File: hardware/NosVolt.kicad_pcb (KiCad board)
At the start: 4 copper layers, 145 x 60 mm, 101 parts, among them CN201 100nF, J101 INPUTS, J102 OUTPUTS, J201 BAT_SENSE, J202 BAT_NTC, J401 USB_C_Receptacle_USB2.0_16P, Q1101 2N7002, Q1102 AO4407A, Q801 2N7002, Q802 AO4407A, Q901 2N7002, Q902 AO4407A, SW101 SW_Reset, SW102 SSSS811101, U1001 INA226, U101 ESP32-S3-WROOM-1, U102 GMT028-05, U1201 INA226, U201 ADS1115IDGS, U301 MP2307DN-LF-Z, U401 AP7361-33ER-13, U402 USBLC6-2SC6, U501 INA226, U601 INA226, U701 INA226

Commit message: rc
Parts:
- added H101: MountingHole, MountingHole:MountingHole_3.2mm_M3_Pad_Via, F.Cu at (108.7, 43.8)
- added H102: MountingHole, MountingHole:MountingHole_3.2mm_M3_Pad_Via, F.Cu at (236.7, 43.8)
- added H103: MountingHole, MountingHole:MountingHole_3.2mm_M3_Pad_Via, F.Cu at (108.7, 91.8)
- added H104: MountingHole, MountingHole:MountingHole_3.2mm_M3_Pad_Via, F.Cu at (236.4, 91.8)
- moved R103 73.6 mm to (226.2, 63.0)
- moved SW101 72.5 mm to (238.7, 50.8)
- moved C101 70.6 mm to (238.7, 54.8), turned to 0 degrees
- moved R104 68.4 mm to (218.4, 63.1), turned to 180 degrees
- moved R102 62.7 mm to (238.7, 57.8), turned to 180 degrees
- moved C401 53.5 mm to (232.7, 52.4)
- moved R101 43.1 mm to (217.1, 88.2)
- moved U101 11.3 mm to (226.6, 75.7)
- moved R401 5.91 mm to (232.4, 48.2)
- moved J101 4.90 mm to (143.6, 44.3)
- moved C802 4.81 mm to (176.6, 62.2)
- moved R402 4.66 mm to (216.6, 46.5)
- moved C601 3.56 mm to (104.9, 72.6)
- moved C602 3.56 mm to (109.9, 72.6)
- moved C701 3.56 mm to (114.7, 72.6)
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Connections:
- SW102 pad 1: unconnected-(SW102-Pad1) -> /USB_LDO/USB_3V3
- U101 pad 28: unconnected-(U101-SPIIO6/GPIO35/FSPID/SUBSPID-Pad28) -> EN_OUT1
- U101 pad 29: unconnected-(U101-SPIIO7/GPIO36/FSPICLK/SUBSPICLK-Pad29) -> EN_OUT2
- U101 pad 30: unconnected-(U101-SPIDQS/GPIO37/FSPIQ/SUBSPIQ-Pad30) -> EN_OUT3
- U101 pad 4: EN_OUT1 -> unconnected-(U101-GPIO4/TOUCH4/ADC1_CH3-Pad4)
- U101 pad 5: EN_OUT2 -> unconnected-(U101-GPIO5/TOUCH5/ADC1_CH4-Pad5)
- U101 pad 6: EN_OUT3 -> unconnected-(U101-GPIO6/TOUCH6/ADC1_CH5-Pad6)
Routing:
- net +3.3V: track 50.8 -> 347.6 mm, vias 0 -> 9
- net SDA: track 0.00 -> 198.1 mm, vias 0 -> 9
- net SCL: track 0.00 -> 186.6 mm, vias 0 -> 6
- net +12V_UPS: track 70.6 -> 196.7 mm, vias 2 -> 4
- net EN_OUT3: track 0.00 -> 97.2 mm
- net GND: track 47.5 -> 123.1 mm, vias 4 -> 10
- net EN_OUT2: track 0.00 -> 73.5 mm
- net EN_OUT1: track 0.00 -> 49.6 mm
- net /USB_LDO/USB_3V3: track 13.3 -> 43.1 mm
- net /Output3/VOUT: track 5.14 -> 32.4 mm, vias 0 -> 2
- net /MP2307/OUT: track 25.6 -> 52.7 mm, vias 2 -> 4
- net /Output2/VOUT: track 0.00 -> 26.9 mm
- net /INA226_BAT/VIN: track 14.3 -> 41.1 mm
- net /INA226_IN/VIN: track 14.3 -> 40.8 mm
- net /INA226_BAT/VOUT: track 4.29 -> 30.7 mm
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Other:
- board size 145 x 60 mm -> 140 x 60 mm
- board text added: "BAT1"
- board text added: "BAT2"
- board text added: "BAT3"
- board text added: "NTC1"
- board text added: "NTC2"

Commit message: 100*100
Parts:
- moved U101 94.2 mm to (140.4, 113.9), turned to 180 degrees
- moved U102 88.9 mm to (262.0, 72.8)
- moved C301 85.5 mm to (108.1, 85.5)
- moved C302 85.5 mm to (108.1, 90.2)
- moved C305 85.5 mm to (108.1, 80.0)
- moved R301 85.5 mm to (119.6, 92.8)
- moved C303 85.5 mm to (119.7, 88.3)
- moved C304 85.5 mm to (115.8, 88.3)
- moved R302 85.5 mm to (115.8, 92.8)
- moved R304 85.5 mm to (112.3, 88.7)
- moved L301 85.5 mm to (121.0, 82.0)
- moved R303 85.5 mm to (112.4, 92.7)
- moved U301 85.5 mm to (113.2, 82.0)
- moved C101 81.2 mm to (169.2, 96.8)
- moved R102 81.2 mm to (169.2, 99.8)
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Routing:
- net +3.3V: track 347.6 -> 53.4 mm, vias 9 -> 0
- net SDA: track 198.1 -> 4.63 mm, vias 9 -> 2
- net SCL: track 186.6 -> 0.00 mm, vias 6 -> 0
- net +12V_UPS: track 196.7 -> 26.5 mm, vias 4 -> 0
- net EN_OUT3: track 97.2 -> 0.00 mm
- net GND: track 123.1 -> 34.8 mm, vias 10 -> 4
- net EN_OUT2: track 73.5 -> 0.00 mm
- net /MP2307/OUT: track 52.7 -> 0.00 mm, vias 4 -> 0
- net EN_OUT1: track 49.6 -> 0.00 mm
- net /USB_LDO/USB_3V3: track 43.1 -> 0.00 mm
- net /INA226_BAT/VIN: track 41.1 -> 7.43 mm
- net /INA226_IN/VIN: track 40.8 -> 7.35 mm
- net /Output3/VOUT: track 32.4 -> 0.00 mm, vias 2 -> 0
- net /INA226_BAT/VOUT: track 30.7 -> 0.00 mm
- net /Output1/VOUT: track 30.5 -> 0.00 mm
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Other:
- board size 140 x 60 mm -> 100 x 60 mm

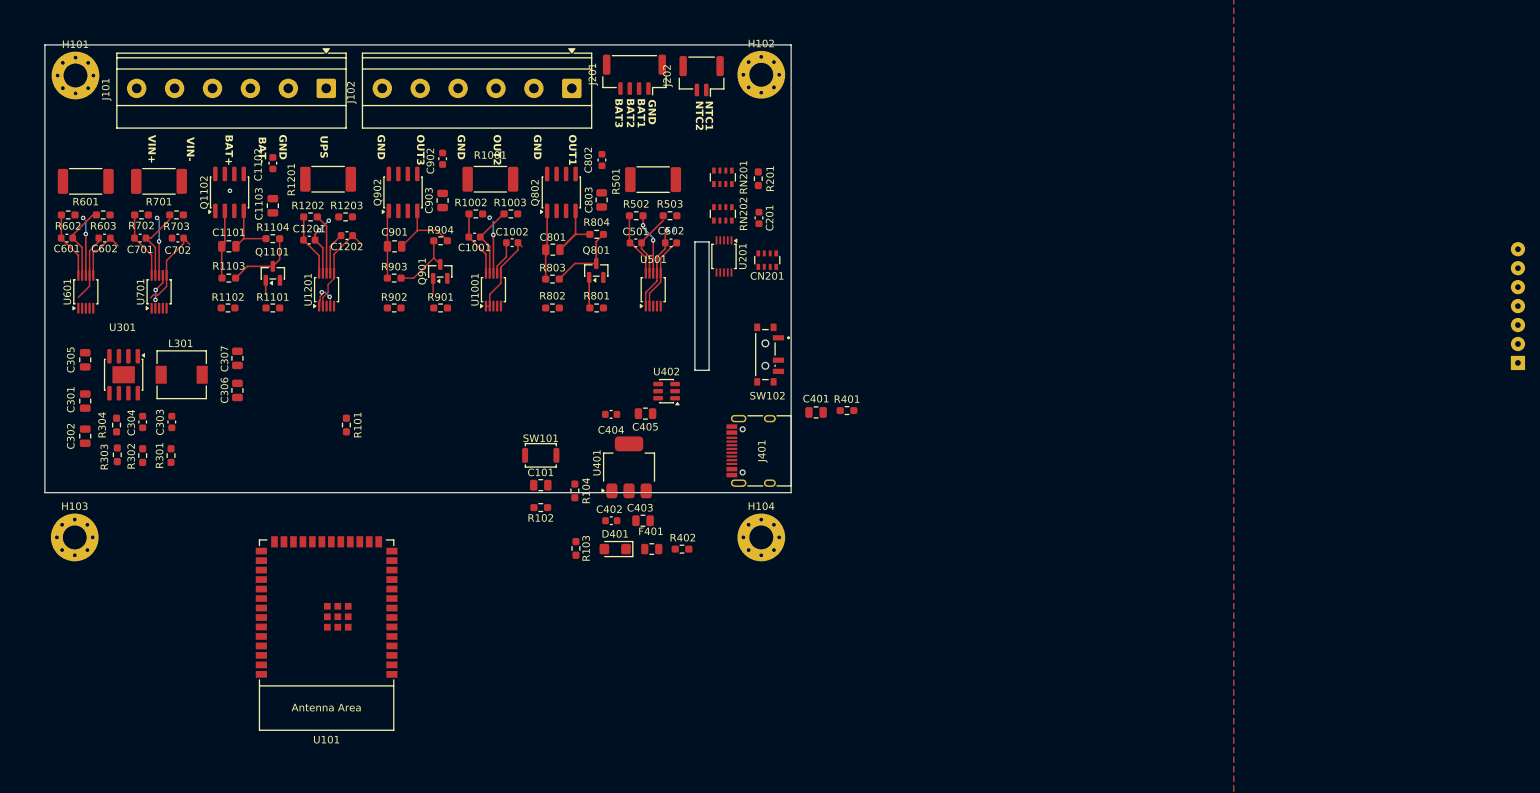
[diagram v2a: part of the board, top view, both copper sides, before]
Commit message: esp32 c3 mini
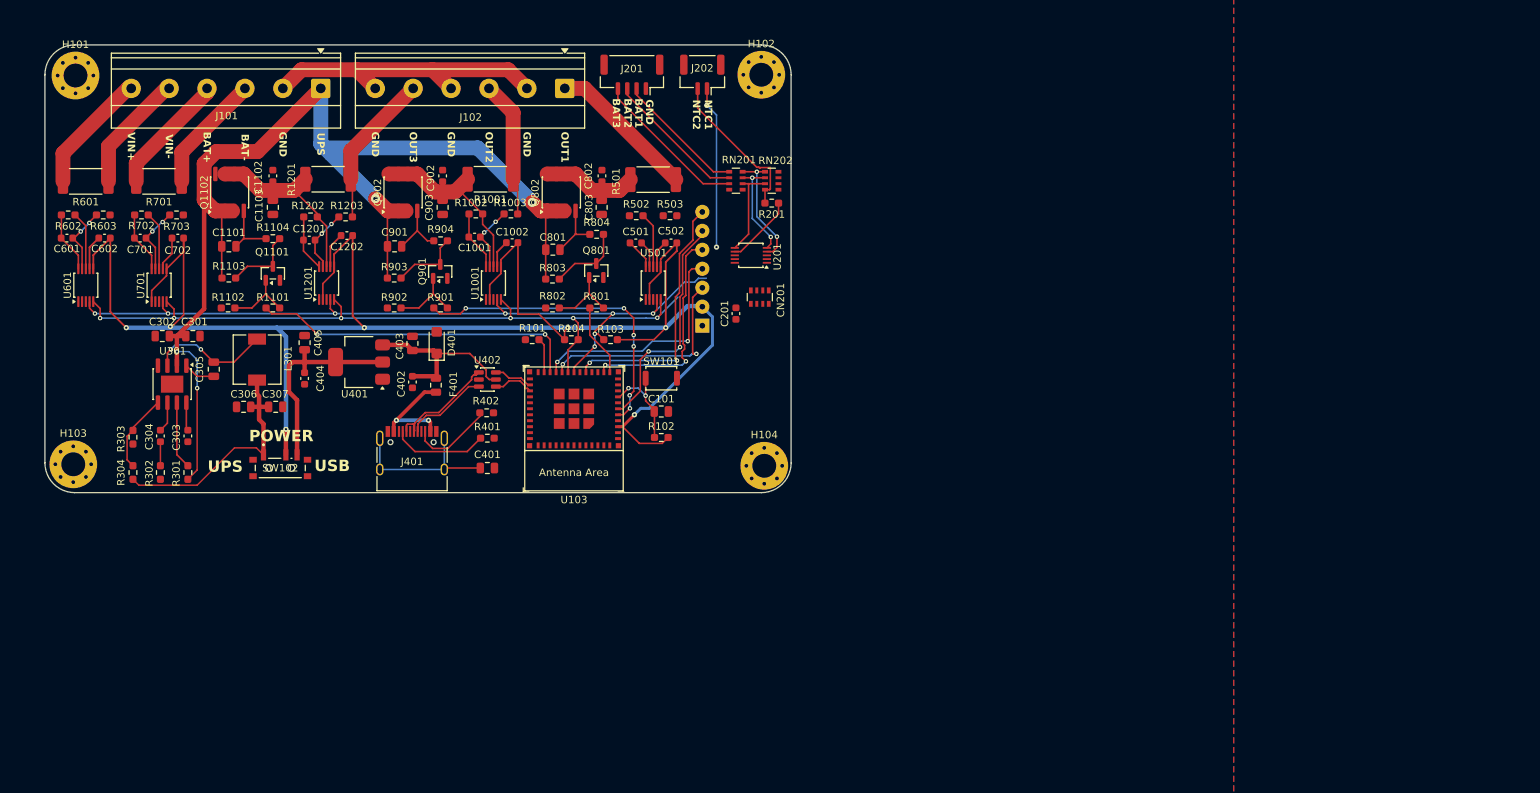
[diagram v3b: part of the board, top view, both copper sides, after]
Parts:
- removed U101: ESP32-S3-WROOM-1, PCM_Espressif:ESP32-S3-WROOM-1
- added U103: ESP32-C3-MINI-1, PCM_Espressif:ESP32-C3-MINI-1, F.Cu at (173.6, 89.3)
- moved U102 109.4 mm to (152.7, 67.8)
- moved SW102 66.8 mm to (134.2, 94.5), turned to 0 degrees
- moved R401 48.3 mm to (162.0, 90.5), turned to 0 degrees
- moved J401 46.9 mm to (151.9, 93.6), turned to 0 degrees
- moved C405 46.7 mm to (137.5, 77.7), turned to 90 degrees
- moved C401 44.7 mm to (162.0, 94.5), turned to 0 degrees
- moved C404 41.4 mm to (137.5, 82.5), turned to -90 degrees
- moved C403 39.0 mm to (151.9, 77.8), turned to 90 degrees
- moved U401 38.8 mm to (144.8, 80.3), turned to 180 degrees
- moved D401 36.6 mm to (155.2, 77.7), turned to 90 degrees
- moved F401 36.3 mm to (155.1, 83.4), turned to 90 degrees
- moved C402 32.5 mm to (151.9, 83.0), turned to -90 degrees
- moved R402 31.9 mm to (161.9, 87.1), turned to 0 degrees
- moved R103 28.4 mm to (178.5, 77.3), turned to 180 degrees
- moved R101 27.4 mm to (168.0, 77.3), turned to 180 degrees
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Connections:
- SW102 pad 1: /USB_LDO/USB_3V3 -> /MP2307/OUT
- SW102 pad 3: /MP2307/OUT -> /USB_LDO/USB_3V3
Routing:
- net +3.3V: track 53.4 -> 269.3 mm, vias 0 -> 9
- net +12V_UPS: track 26.5 -> 161.1 mm, vias 0 -> 4
- net SDA: track 4.63 -> 105.8 mm, vias 2 -> 8
- net SCL: track 0.00 -> 100.5 mm, vias 0 -> 6
- net EN_OUT3: track 0.00 -> 44.2 mm, vias 0 -> 2
- net EN_OUT2: track 0.00 -> 42.3 mm, vias 0 -> 6
- net SPI_CS_TFT: track 0.00 -> 34.8 mm, vias 0 -> 2
- net /MP2307/OUT: track 0.00 -> 33.1 mm
- net SPI_MOSI: track 0.00 -> 31.4 mm, vias 0 -> 2
- net TFT_DC: track 0.00 -> 31.0 mm, vias 0 -> 2
- net SPI_SCLK: track 0.00 -> 29.4 mm, vias 0 -> 2
- net TFT_RST: track 0.00 -> 29.3 mm, vias 0 -> 2
- net GND: track 34.8 -> 63.2 mm, vias 4 -> 0
- net /USB_LDO/USB_3V3: track 0.00 -> 28.2 mm
- net /USB_LDO/USB_5V: track 0.00 -> 24.2 mm
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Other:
- outline, holes or cut-outs redrawn
- board text added: "POWER"
- board text added: "USB"

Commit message: thermal relief
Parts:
- removed C1103, C803, C903: 22uF, Capacitor_SMD:C_0805_2012Metric
- removed U103: ESP32-C3-MINI-1, PCM_Espressif:ESP32-C3-MINI-1
- added C102: 100nF, Capacitor_SMD:C_0603_1608Metric, F.Cu at (139.6, 88.0)
- added C103: 22uF, Capacitor_SMD:C_0805_2012Metric, F.Cu at (143.4, 87.9)
- added NT1001: NetTie_SHUNT_IN_SENSE, NetTie:NetTie-2_SMD_Pad0.5mm, F.Cu at (173.6, 56.3)
- added NT1002: NetTie_SHUNT_OUT_SENSE, NetTie:NetTie-2_SMD_Pad0.5mm, F.Cu at (179.6, 56.6)
- added NT101: NetTie_OUT_12V, NetTie:NetTie-2_SMD_Pad0.5mm, F.Cu at (161.3, 58.6)
- added NT1201: NetTie_SHUNT_IN_SENSE, NetTie:NetTie-2_SMD_Pad0.5mm, F.Cu at (152.7, 56.7)
- added NT1202: NetTie_SHUNT_OUT_SENSE, NetTie:NetTie-2_SMD_Pad0.5mm, F.Cu at (157.8, 56.3)
- added NT301: NetTie_SW_BS, NetTie:NetTie-2_SMD_Pad0.5mm, F.Cu at (183.7, 80.7)
- added NT302: NetTie_SW_FB, NetTie:NetTie-2_SMD_Pad0.5mm, F.Cu at (182.9, 86.5)
- added NT303: NetTie_IN_EN, NetTie:NetTie-2_SMD_Pad0.5mm, F.Cu at (185.6, 78.3)
- added NT304: NetTie_GND, NetTie:NetTie-2_SMD_Pad0.5mm, F.Cu at (188.8, 82.0)
- added NT501: NetTie_SHUNT_IN_SENSE, NetTie:NetTie-2_SMD_Pad0.5mm, F.Cu at (195.9, 56.7)
- added NT502: NetTie_SHUNT_OUT_SENSE, NetTie:NetTie-2_SMD_Pad0.5mm, F.Cu at (200.8, 56.4)
- added NT601: NetTie_SHUNT_IN_SENSE, NetTie:NetTie-2_SMD_Pad0.5mm, F.Cu at (121.3, 56.3)
- added NT602: NetTie_SHUNT_OUT_SENSE, NetTie:NetTie-2_SMD_Pad0.5mm, F.Cu at (127.9, 56.3)
- added NT701: NetTie_SHUNT_IN_SENSE, NetTie:NetTie-2_SMD_Pad0.5mm, F.Cu at (131.3, 55.3)
- added NT702: NetTie_SHUNT_OUT_SENSE, NetTie:NetTie-2_SMD_Pad0.5mm, F.Cu at (137.4, 55.5)
- added U101: GMT028-05, NosLib:GMT028-05, F.Cu at (49.1, 81.8)
- C1101, C801, C901: value 22nF -> 100nF; footprint Capacitor_SMD:C_0805_2012Metric -> Capacitor_SMD:C_0603_1608Metric
- C1102, C802, C902: value 100nF -> 22uF; footprint Capacitor_SMD:C_0603_1608Metric -> Capacitor_SMD:C_0805_2012Metric
- U102: value GMT028-05 -> ESP32-S3-WROOM-1; footprint NosLib:GMT028-05 -> PCM_Espressif:ESP32-S3-WROOM-1; moved to F.Cu
- U301: footprint Package_SO:SOIC-8-1EP_3.9x4.9mm_P1.27mm_EP2.29x3mm -> Package_SO:SOIC-8-1EP_3.9x4.9mm_P1.27mm_EP2.29x3mm_ThermalVias
- moved U201 92.0 mm to (105.3, 65.2), turned to -90 degrees
- moved R201 90.1 mm to (110.0, 58.3)
- moved RN201 90.0 mm to (105.3, 53.7)
- moved RN202 90.0 mm to (110.1, 53.7)
- moved CN201 88.8 mm to (110.1, 62.8), turned to 0 degrees
- moved R303 86.2 mm to (200.6, 86.5), turned to 180 degrees
- moved C201 85.4 mm to (110.2, 67.4), turned to 0 degrees
- moved R302 83.4 mm to (200.6, 82.5), turned to 180 degrees
- moved R304 81.8 mm to (195.8, 86.5), turned to 0 degrees
- moved R301 80.5 mm to (200.6, 78.5), turned to 180 degrees
- moved C304 78.0 mm to (195.8, 82.5), turned to 0 degrees
- moved C303 74.9 mm to (195.8, 78.5), turned to 0 degrees
- moved C305 70.8 mm to (195.8, 74.9), turned to 180 degrees
- moved U301 70.0 mm to (189.7, 80.5), turned to 0 degrees
- moved J202 65.8 mm to (125.0, 41.2)
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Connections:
- net +3.3V renamed +3V3
- C1101 pad 1: Net-(Q1102-G) -> /Output3/SHUNT_DRAIN
- C1101 pad 2: +12V_UPS -> GND
- C1102 pad 1: /Output3/INA226_OUT/VIN -> /Output3/SHUNT_DRAIN
- C301 pad 1: +12V_UPS -> /+12V_UPS
- C301 pad 2: GND -> /MP2307/PWR_GND
- C302 pad 1: +12V_UPS -> /+12V_UPS
- C302 pad 2: GND -> /MP2307/PWR_GND
- C305 pad 2: Net-(U301-SW) -> Net-(C305-Pad2)
- C306 pad 1: /MP2307/OUT -> +3V3_UPS
- C306 pad 2: GND -> /MP2307/PWR_GND
- C307 pad 1: /MP2307/OUT -> +3V3_UPS
- C307 pad 2: GND -> /MP2307/PWR_GND
- C404 pad 1: /USB_LDO/USB_3V3 -> +3V3_USB
- C405 pad 1: /USB_LDO/USB_3V3 -> +3V3_USB
- C801 pad 1: Net-(Q802-G) -> /Output1/SHUNT_DRAIN
- C801 pad 2: +12V_UPS -> GND
- C802 pad 1: /Output1/INA226_OUT/VIN -> /Output1/SHUNT_DRAIN
- C901 pad 1: Net-(Q902-G) -> /Output2/SHUNT_DRAIN
- C901 pad 2: +12V_UPS -> GND
- C902 pad 1: /Output2/INA226_OUT/VIN -> /Output2/SHUNT_DRAIN
- J101 pad 1: +12V_UPS -> /SHUNT_OUT_LO
- J101 pad 2: GND -> /SHUNT_OUT_HI
- J101 pad 3: /INA226_BAT/VOUT -> /SHUNT_BAT_LO
- J101 pad 4: /INA226_BAT/VIN -> /SHUNT_BAT_HI
- J101 pad 5: /INA226_IN/VOUT -> /SHUNT_IN_LO
- J101 pad 6: /INA226_IN/VIN -> /SHUNT_IN_HI
- J102 pad 2: GND -> /SHUNT_OUT_HI
- J102 pad 4: GND -> /SHUNT_OUT_HI
- J102 pad 6: GND -> /SHUNT_OUT_HI
- L301 pad 1: Net-(U301-SW) -> /MP2307/SW
- L301 pad 2: /MP2307/OUT -> +3V3_UPS
- Q1102 pad 1: +12V_UPS -> /SHUNT_OUT_LO
- Q1102 pad 2: +12V_UPS -> /SHUNT_OUT_LO
- Q1102 pad 3: +12V_UPS -> /SHUNT_OUT_LO
- Q1102 pad 5: /Output3/INA226_OUT/VIN -> /Output3/SHUNT_DRAIN
- Q1102 pad 6: /Output3/INA226_OUT/VIN -> /Output3/SHUNT_DRAIN
- Q1102 pad 7: /Output3/INA226_OUT/VIN -> /Output3/SHUNT_DRAIN
- Q1102 pad 8: /Output3/INA226_OUT/VIN -> /Output3/SHUNT_DRAIN
- Q802 pad 1: +12V_UPS -> /SHUNT_OUT_LO
- Q802 pad 2: +12V_UPS -> /SHUNT_OUT_LO
- Q802 pad 3: +12V_UPS -> /SHUNT_OUT_LO
- Q802 pad 5: /Output1/INA226_OUT/VIN -> /Output1/SHUNT_DRAIN
- Q802 pad 6: /Output1/INA226_OUT/VIN -> /Output1/SHUNT_DRAIN
- Q802 pad 7: /Output1/INA226_OUT/VIN -> /Output1/SHUNT_DRAIN
- Q802 pad 8: /Output1/INA226_OUT/VIN -> /Output1/SHUNT_DRAIN
- Q902 pad 1: +12V_UPS -> /SHUNT_OUT_LO
- Q902 pad 2: +12V_UPS -> /SHUNT_OUT_LO
- Q902 pad 3: +12V_UPS -> /SHUNT_OUT_LO
- Q902 pad 5: /Output2/INA226_OUT/VIN -> /Output2/SHUNT_DRAIN
- Q902 pad 6: /Output2/INA226_OUT/VIN -> /Output2/SHUNT_DRAIN
- Q902 pad 7: /Output2/INA226_OUT/VIN -> /Output2/SHUNT_DRAIN
- Q902 pad 8: /Output2/INA226_OUT/VIN -> /Output2/SHUNT_DRAIN
- R1001 pad 2: /Output2/INA226_OUT/VIN -> /Output2/SHUNT_DRAIN
- R1002 pad 1: /Output2/INA226_OUT/VIN -> Net-(U1001-Vbus)
- R1003 pad 1: /Output2/VOUT -> Net-(NT1002-Pad2)
- R1103 pad 2: +12V_UPS -> /SHUNT_OUT_LO
- R1201 pad 2: /Output3/INA226_OUT/VIN -> /Output3/SHUNT_DRAIN
- R1202 pad 1: /Output3/INA226_OUT/VIN -> Net-(U1201-Vbus)
- R1203 pad 1: /Output3/VOUT -> Net-(NT1202-Pad2)
- R301 pad 1: +12V_UPS -> Net-(NT303-Pad2)
- R304 pad 2: /MP2307/OUT -> Net-(NT302-Pad1)
- R501 pad 2: /Output1/INA226_OUT/VIN -> /Output1/SHUNT_DRAIN
- R502 pad 1: /Output1/INA226_OUT/VIN -> Net-(U501-Vbus)
- R503 pad 1: /Output1/VOUT -> Net-(NT502-Pad2)
- R601 pad 1: /INA226_IN/VOUT -> /SHUNT_IN_LO
- R601 pad 2: /INA226_IN/VIN -> /SHUNT_IN_HI
- R602 pad 1: /INA226_IN/VIN -> Net-(U601-Vbus)
- R603 pad 1: /INA226_IN/VOUT -> Net-(NT602-Pad2)
- R701 pad 1: /INA226_BAT/VOUT -> /SHUNT_BAT_LO
- R701 pad 2: /INA226_BAT/VIN -> /SHUNT_BAT_HI
- R702 pad 1: /INA226_BAT/VIN -> Net-(U701-Vbus)
- R703 pad 1: /INA226_BAT/VOUT -> Net-(NT702-Pad2)
- R803 pad 2: +12V_UPS -> /SHUNT_OUT_LO
- R903 pad 2: +12V_UPS -> /SHUNT_OUT_LO
- SW102 pad 1: /MP2307/OUT -> +3V3_USB
- SW102 pad 3: /USB_LDO/USB_3V3 -> +3V3_UPS
- U1001 pad 8: /Output2/INA226_OUT/VIN -> Net-(U1001-Vbus)
- U102 pad 3: SPI_SCLK -> EN
- U102 pad 4: SPI_MOSI -> EN_OUT3
- U102 pad 5: TFT_RST -> EN_OUT2
- U102 pad 6: TFT_DC -> EN_OUT1
- U102 pad 7: SPI_CS_TFT -> unconnected-(U102-GPIO7/TOUCH7/ADC1_CH6-Pad7)
- U1201 pad 8: /Output3/INA226_OUT/VIN -> Net-(U1201-Vbus)
- U301 pad 2: +12V_UPS -> /+12V_UPS
- U301 pad 3: Net-(U301-SW) -> /MP2307/SW
- U301 pad 9: GND -> /MP2307/PWR_GND
- U401 pad 2: /USB_LDO/USB_3V3 -> +3V3_USB
- U501 pad 8: /Output1/INA226_OUT/VIN -> Net-(U501-Vbus)
- U601 pad 8: /INA226_IN/VIN -> Net-(U601-Vbus)
- U701 pad 8: /INA226_BAT/VIN -> Net-(U701-Vbus)
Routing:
- net +12V_UPS: track 161.1 -> 0.00 mm, vias 4 -> 0
- net +3V3: track 269.3 -> 159.8 mm, vias 9 -> 6
- net EN_OUT3: track 44.2 -> 0.00 mm, vias 2 -> 0
- net EN_OUT2: track 42.3 -> 0.00 mm, vias 6 -> 0
- net /SHUNT_OUT_HI: track 0.00 -> 41.8 mm
- net /SHUNT_OUT_LO: track 0.00 -> 41.7 mm, vias 0 -> 2
- net /+12V_UPS: track 0.00 -> 39.6 mm
- net /MP2307/OUT: track 33.1 -> 0.00 mm
- net GND: track 63.2 -> 31.2 mm, vias 0 -> 2
- net SCL: track 100.5 -> 130.4 mm, vias 6 -> 7
- net /USB_LDO/USB_3V3: track 28.2 -> 0.00 mm
- net /Output2/INA226_OUT/VIN: track 27.3 -> 0.00 mm
- net /Output3/INA226_OUT/VIN: track 26.8 -> 0.00 mm
- net /INA226_IN/VIN: track 24.3 -> 0.00 mm
- net /USB_LDO/USB_5V: track 24.2 -> 0.00 mm
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- added copper zone on F.Cu, net /MP2307/PWR_GND
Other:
- outline, holes or cut-outs redrawn

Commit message: optimization
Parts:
- moved R304 6.54 mm to (189.3, 86.2), turned to -90 degrees
- moved R303 5.75 mm to (194.9, 86.2), turned to 90 degrees
- moved R302 4.98 mm to (198.6, 87.1), turned to 0 degrees
- moved C303 4.26 mm to (198.6, 75.2)
- moved C307 3.40 mm to (179.3, 90.7), turned to -90 degrees
- moved C304 2.80 mm to (198.6, 83.1)
- moved NT301 2.56 mm to (186.3, 80.6)
- moved C301 2.56 mm to (182.9, 76.2)
- moved C302 2.56 mm to (186.6, 76.2)
- moved L301 2.56 mm to (184.3, 84.0)
- moved NT302 2.56 mm to (185.5, 86.5)
- moved NT304 2.56 mm to (191.4, 82.0)
- moved U301 2.56 mm to (192.3, 80.5)
- moved R301 2.14 mm to (198.6, 79.2)
- moved C305 1.57 mm to (194.3, 75.5)
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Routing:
- net Net-(NT302-Pad1): track 14.3 -> 3.56 mm, vias 2 -> 0
- net GND: track 31.2 -> 23.2 mm
- net +3V3_UPS: track 6.74 -> 13.9 mm
- net Net-(U301-EN): track 8.08 -> 3.21 mm
- net Net-(U301-SS): track 0.00 -> 4.67 mm
- net Net-(C305-Pad2): track 14.1 -> 9.88 mm
- net Net-(NT303-Pad2): track 16.3 -> 12.5 mm
- net /+12V_UPS: track 39.6 -> 42.8 mm
- net Net-(U301-FB): track 10.6 -> 8.38 mm, vias 0 -> 2
- net Net-(U301-BS): track 11.5 -> 10.6 mm
- net Net-(C304-Pad2): track 3.07 -> 4.00 mm
- net SCL: vias 7 -> 6

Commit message: tracing
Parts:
- U101: moved to B.Cu
- moved U101 105.3 mm to (152.7, 62.7)
- moved C301 1.99 mm to (181.7, 77.8)
- moved NT501 1.98 mm to (194.5, 55.3), turned to -90 degrees
- moved C302 1.84 mm to (185.7, 77.8)
- moved U1201 1.64 mm to (156.2, 66.5), turned to 180 degrees
- moved U501 1.55 mm to (198.3, 66.5), turned to 180 degrees
- moved NT1201 1.33 mm to (152.4, 55.4), turned to -90 degrees
- moved NT1002 1.30 mm to (179.5, 55.3), turned to -90 degrees
- moved U1001 1.30 mm to (176.9, 66.5), turned to 180 degrees
- moved NT1202 1.25 mm to (158.4, 55.2), turned to -90 degrees
- moved NT602 1.23 mm to (127.3, 55.2), turned to -90 degrees
- moved NT502 1.02 mm to (200.6, 55.4), turned to -90 degrees
- moved NT1001 1.02 mm to (173.4, 55.3), turned to -90 degrees
- moved NT601 0.90 mm to (121.3, 55.4), turned to -90 degrees
- moved NT303 0.71 mm to (187.6, 79.0), turned to 90 degrees
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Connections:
- net /Output1/VOUT renamed /SHUNT_OUT_LO1
- net /Output2/VOUT renamed /SHUNT_OUT_LO2
- net /Output3/VOUT renamed /SHUNT_OUT_LO3
- R1103 pad 2: /SHUNT_OUT_LO -> Net-(NT1101-Pad1)
- R803 pad 2: /SHUNT_OUT_LO -> Net-(NT801-Pad1)
- R903 pad 2: /SHUNT_OUT_LO -> Net-(NT901-Pad1)
- U102 pad 4: EN_OUT3 -> EN_OUT1
- U102 pad 6: EN_OUT1 -> EN_OUT3
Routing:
- net +3V3: track 159.8 -> 306.5 mm, vias 6 -> 19
- net EN_OUT1: track 0.00 -> 64.4 mm, vias 0 -> 2
- net EN_OUT2: track 0.00 -> 42.3 mm, vias 0 -> 2
- net /SHUNT_OUT_LO: track 41.7 -> 83.1 mm, vias 2 -> 3
- net /USB_LDO/USB_5V: track 0.00 -> 33.6 mm, vias 0 -> 2
- net GND: track 23.2 -> 54.0 mm, vias 2 -> 4
- net SDA: track 125.9 -> 151.6 mm, vias 7 -> 9
- net Net-(J202-Pin_2): track 0.00 -> 25.0 mm
- net EN_OUT3: track 0.00 -> 22.6 mm, vias 0 -> 2
- net EN: track 0.00 -> 22.4 mm, vias 0 -> 2
- net SCL: track 130.4 -> 151.6 mm, vias 6 -> 8
- net Net-(J401-SHIELD): track 0.00 -> 20.9 mm
- net Net-(RN201-R2.2): track 0.00 -> 20.8 mm, vias 0 -> 4
- net Net-(RN201-R3.2): track 0.00 -> 20.8 mm, vias 0 -> 2
- net Net-(RN201-R1.2): track 0.00 -> 20.1 mm, vias 0 -> 2
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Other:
- copper layers 4 -> 2

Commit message: fix errors
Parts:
- added NT1101: NetTie_2, NetTie:NetTie-2_SMD_Pad0.5mm, F.Cu at (141.2, 59.2)
- added NT801: NetTie_2, NetTie:NetTie-2_SMD_Pad0.5mm, F.Cu at (183.4, 58.9)
- added NT901: NetTie_2, NetTie:NetTie-2_SMD_Pad0.5mm, F.Cu at (162.4, 58.8)
- NT301: value NetTie_SW_BS -> NetTie_IN_EN
- NT302: value NetTie_SW_FB -> NetTie_GND
- NT303: value NetTie_IN_EN -> NetTie_SW_BS
- NT304: value NetTie_GND -> NetTie_SW_FB
- moved NT304 7.47 mm to (185.5, 86.5), turned to 180 degrees
- moved NT302 7.44 mm to (191.4, 82.0), turned to 90 degrees
- moved NT303 2.17 mm to (186.2, 80.7), turned to -90 degrees
- moved NT301 2.12 mm to (187.6, 79.0), turned to 90 degrees
- moved C201 0.70 mm to (110.9, 67.4)
- moved CN201 0.70 mm to (110.8, 62.8)
- moved R201 0.70 mm to (110.7, 58.3)
- moved RN201 0.70 mm to (106.4, 53.7)
- moved RN202 0.70 mm to (110.8, 53.7)
- moved U201 0.70 mm to (106.0, 65.2)
- moved NT1202 0.55 mm to (158.4, 55.8)
- moved C1102 0.40 mm to (148.6, 53.5)
- moved C1101 0.40 mm to (148.6, 57.8)
- moved NT1201 0.40 mm to (152.4, 55.8)
- moved Q1102 0.40 mm to (143.2, 55.7)
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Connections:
- NT301 pad 1: Net-(C305-Pad2) -> /+12V_UPS
- NT301 pad 2: /MP2307/SW -> Net-(NT301-Pad2)
- NT302 pad 1: Net-(NT302-Pad1) -> GND
- NT302 pad 2: +3V3_UPS -> /MP2307/PWR_GND
- NT303 pad 1: /+12V_UPS -> Net-(C305-Pad2)
- NT303 pad 2: Net-(NT303-Pad2) -> /MP2307/SW
- NT304 pad 1: GND -> Net-(NT304-Pad1)
- NT304 pad 2: /MP2307/PWR_GND -> +3V3_UPS
- R301 pad 1: Net-(NT303-Pad2) -> Net-(NT301-Pad2)
- R304 pad 2: Net-(NT302-Pad1) -> Net-(NT304-Pad1)
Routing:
- net GND: track 54.0 -> 70.9 mm, vias 4 -> 5
- net Net-(NT303-Pad2): track 12.5 -> 0.00 mm, vias 2 -> 0
- net Net-(NT301-Pad2): track 0.00 -> 12.5 mm, vias 0 -> 2
- net Net-(NT801-Pad1): track 0.00 -> 5.63 mm
- net Net-(NT901-Pad1): track 0.00 -> 5.51 mm
- net Net-(NT1101-Pad1): track 0.00 -> 5.18 mm
- net Net-(NT304-Pad1): track 0.00 -> 3.56 mm
- net Net-(NT302-Pad1): track 3.56 -> 0.00 mm
- net +3V3: track 306.5 -> 309.1 mm
- net /SHUNT_IN_LO: track 15.1 -> 17.3 mm
- net Net-(RN201-R2.2): track 20.8 -> 22.4 mm
- net Net-(J202-Pin_2): track 25.0 -> 26.5 mm
- net /SHUNT_OUT_HI: track 41.8 -> 43.4 mm
- net /SHUNT_IN_HI: track 17.0 -> 18.3 mm
- net Net-(U201-AIN3): track 13.3 -> 14.4 mm
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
